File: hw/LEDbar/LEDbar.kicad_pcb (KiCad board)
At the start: 2 copper layers, 42 x 24 mm, 25 parts, among them J1 Conn_01x04, J2 Conn_01x04, J3 Conn_01x04, U1 STP16CP05XT

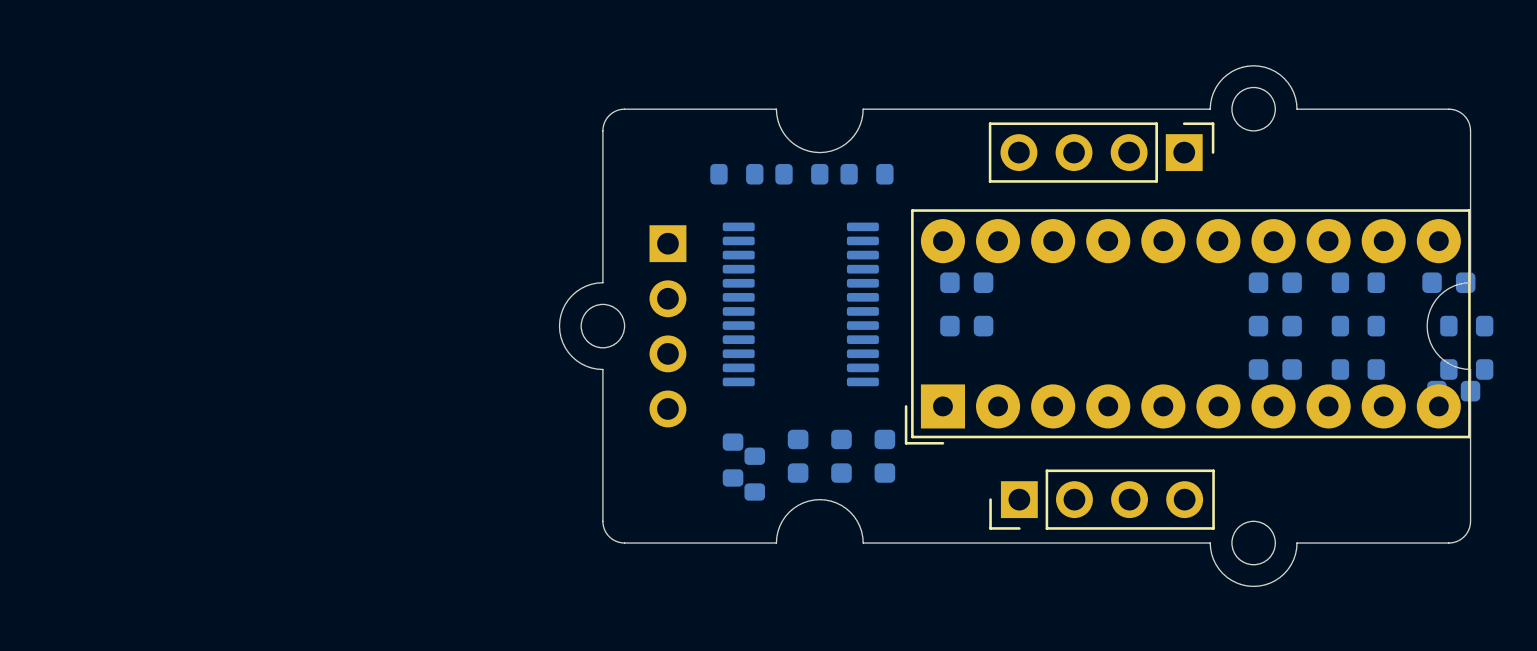
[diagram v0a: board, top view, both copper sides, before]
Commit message: first version of the led bar finished
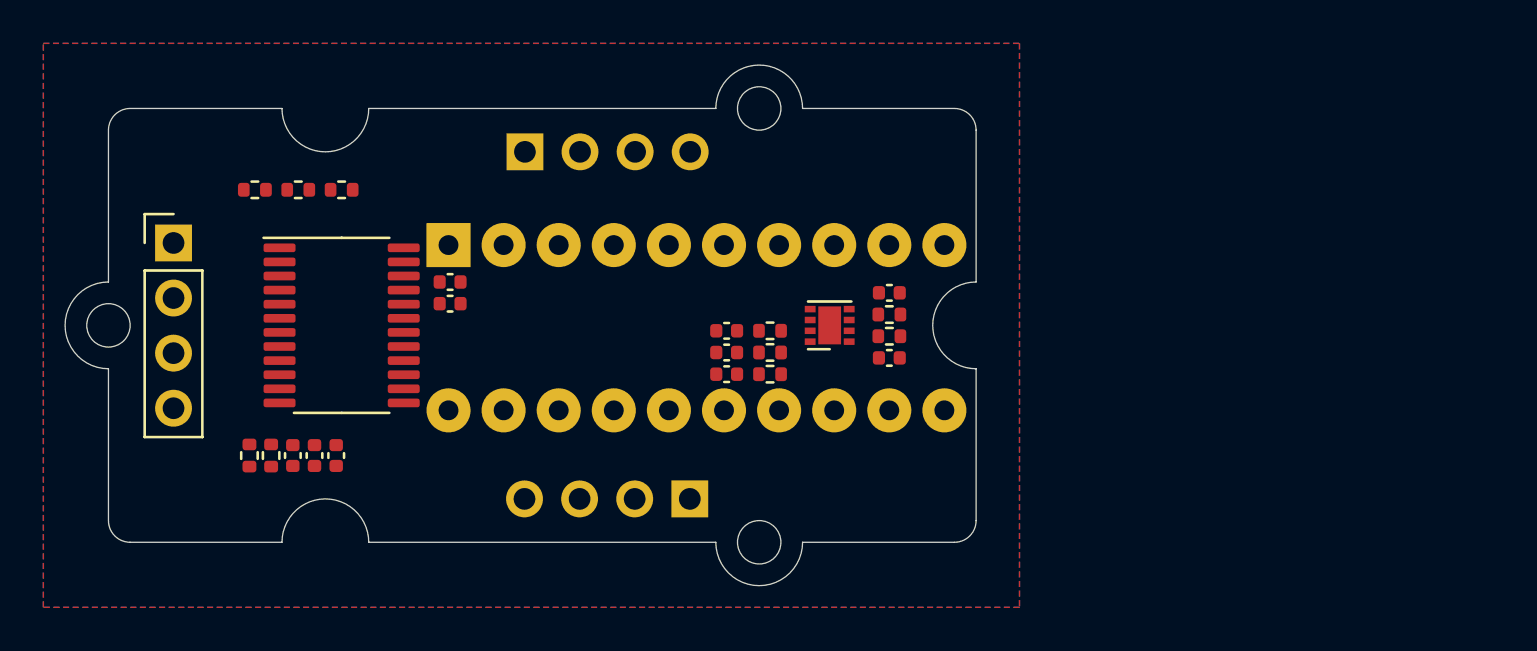
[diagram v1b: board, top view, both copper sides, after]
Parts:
- added U2: LM358_DFN, Package_DFN_QFN:DFN-8-1EP_2x2mm_P0.5mm_EP1.05x1.75mm, F.Cu at (150.5, 100.0)
- BAR1: footprint Display:HDSP-4830 -> Display:HLCP-J100; moved to B.Cu
- C1, C10, C2, C3, C4, C5, C6, C7, C8, C9: footprint Capacitor_SMD:C_0603_1608Metric -> Capacitor_SMD:C_0402_1005Metric; moved to F.Cu
- J1, U1: moved to F.Cu
- J2, J3: moved to B.Cu
- R1, R10, R2, R3, R4, R5, R6, R7, R8, R9: footprint Resistor_SMD:R_0603_1608Metric -> Resistor_SMD:R_0402_1005Metric; moved to F.Cu
- moved J2 30.4 mm to (136.4, 92.0)
- moved R4 27.2 mm to (147.7, 100.2), turned to 0 degrees
- moved R5 27.1 mm to (147.7, 101.2), turned to 0 degrees
- moved R1 27.1 mm to (147.7, 102.2), turned to 0 degrees
- moved R3 26.7 mm to (153.2, 99.5), turned to 0 degrees
- moved R2 26.6 mm to (153.2, 100.5), turned to 0 degrees
- moved C9 26.4 mm to (153.2, 98.5), turned to 0 degrees
- moved C10 26.0 mm to (153.2, 101.5), turned to 0 degrees
- moved C6 25.4 mm to (145.7, 100.2), turned to 0 degrees
- moved C1 25.3 mm to (145.7, 101.2), turned to 0 degrees
- moved C2 25.3 mm to (145.7, 102.2), turned to 0 degrees
- moved C3 25.3 mm to (127.7, 106.0)
- moved C4 24.3 mm to (126.7, 106.0)
- moved R6 24.2 mm to (128.0, 93.7), turned to 0 degrees
- moved BAR1 24.0 mm to (132.9, 96.3), turned to -90 degrees
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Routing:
- added copper zone on B.Cu, net (none)
- added copper zone on F.Cu, net (none)
